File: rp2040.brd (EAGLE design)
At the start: 55 x 25 mm, 58 parts, among them IC1 RP2040-QFN56, J2 1X6_2.5MM, J3 1X6_2.5MM, J4 1X6_2.5MM, J5 1X6_2.5MM, U1 9DoF IMU

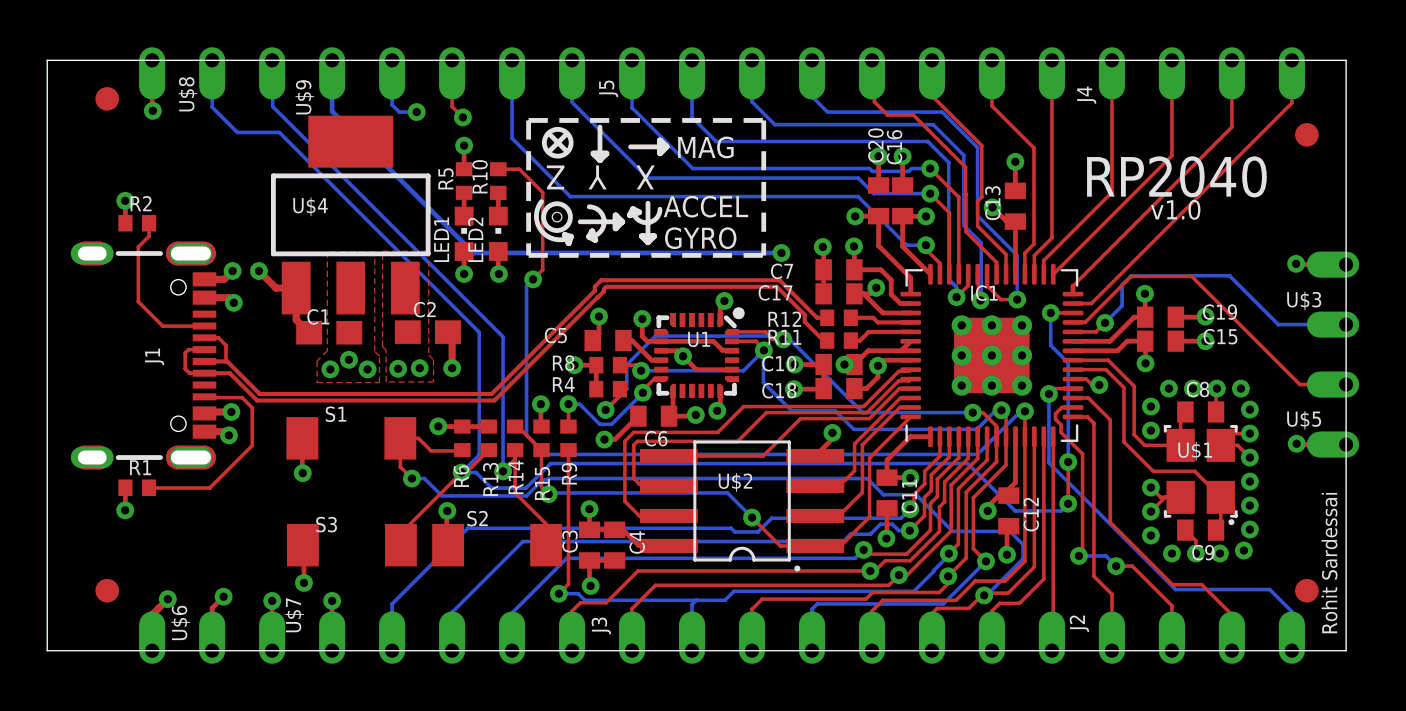
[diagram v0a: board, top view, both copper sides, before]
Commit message: improved traces, reduced vias
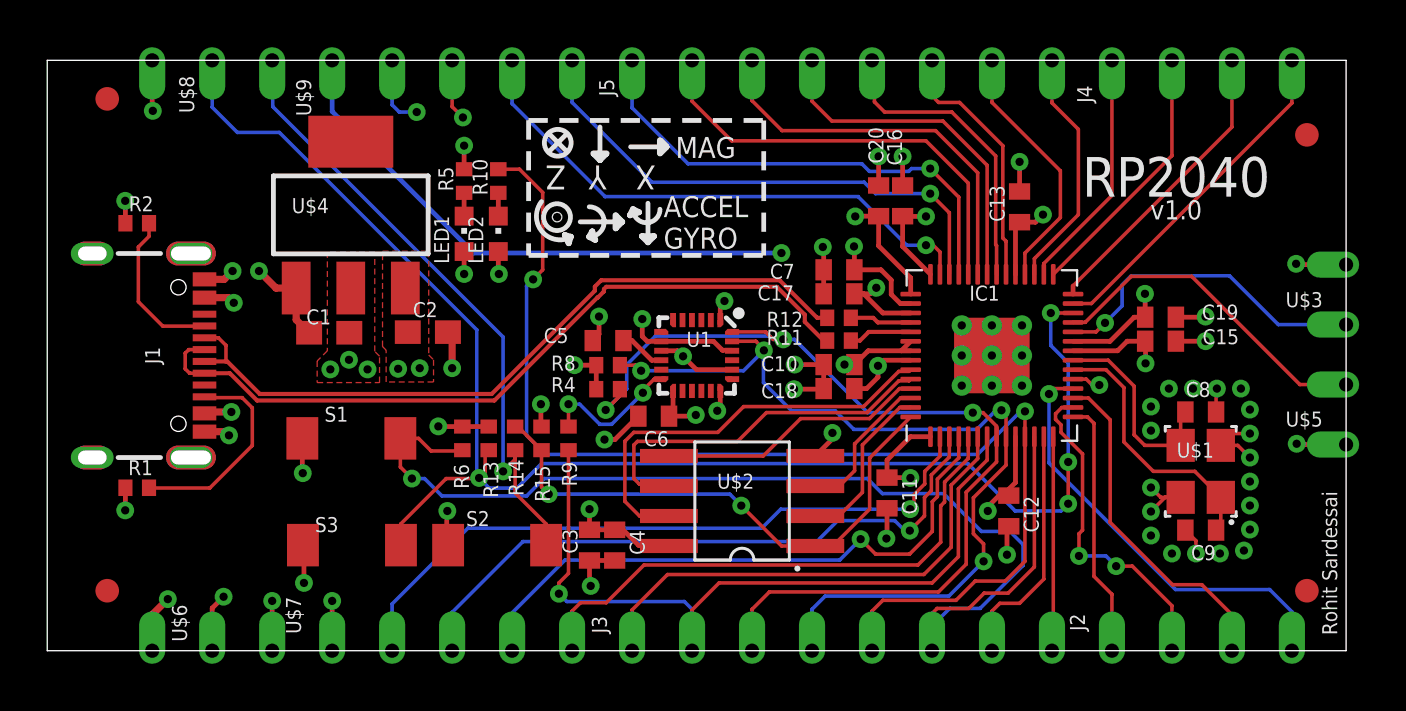
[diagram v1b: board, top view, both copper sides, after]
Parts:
- moved C13 0.18 mm to (41.2, 18.8)
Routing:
- net GPIO9/USR_BUTTON: track 47.6 -> 51.5 mm, vias 2 -> 1
- net GPIO24: track 18.6 -> 14.9 mm, vias 1 -> 0
- net GPIO25: track 19.3 -> 16.8 mm, vias 1 -> 0
- net GPIO26/ADC0: track 21.1 -> 18.7 mm, vias 1 -> 0
- net GPIO5/IMU_INT: track 31.6 -> 33.4 mm, vias 2 -> 1
- net GPIO23: track 11.9 -> 12.9 mm
- net GPIO21: track 9.96 -> 10.9 mm
- net GPIO20: track 9.37 -> 10.3 mm
- net GPIO29/ADC3: track 24.2 -> 23.5 mm
- net GPIO4: track 21.1 -> 21.5 mm, vias 1 -> 0
- net GPIO3: track 23.1 -> 23.4 mm, vias 1 -> 0
- net GPIO6/I2C1_SDA: vias 4 -> 3
